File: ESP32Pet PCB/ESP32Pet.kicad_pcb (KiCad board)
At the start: 2 copper layers, 82.3 x 79 mm, 14 parts, among them J2 3.7V LIPO + CHARGING, U1 3.3V LDO, U2 TFT LCD, U5 ESP32-DEVKIT-V1

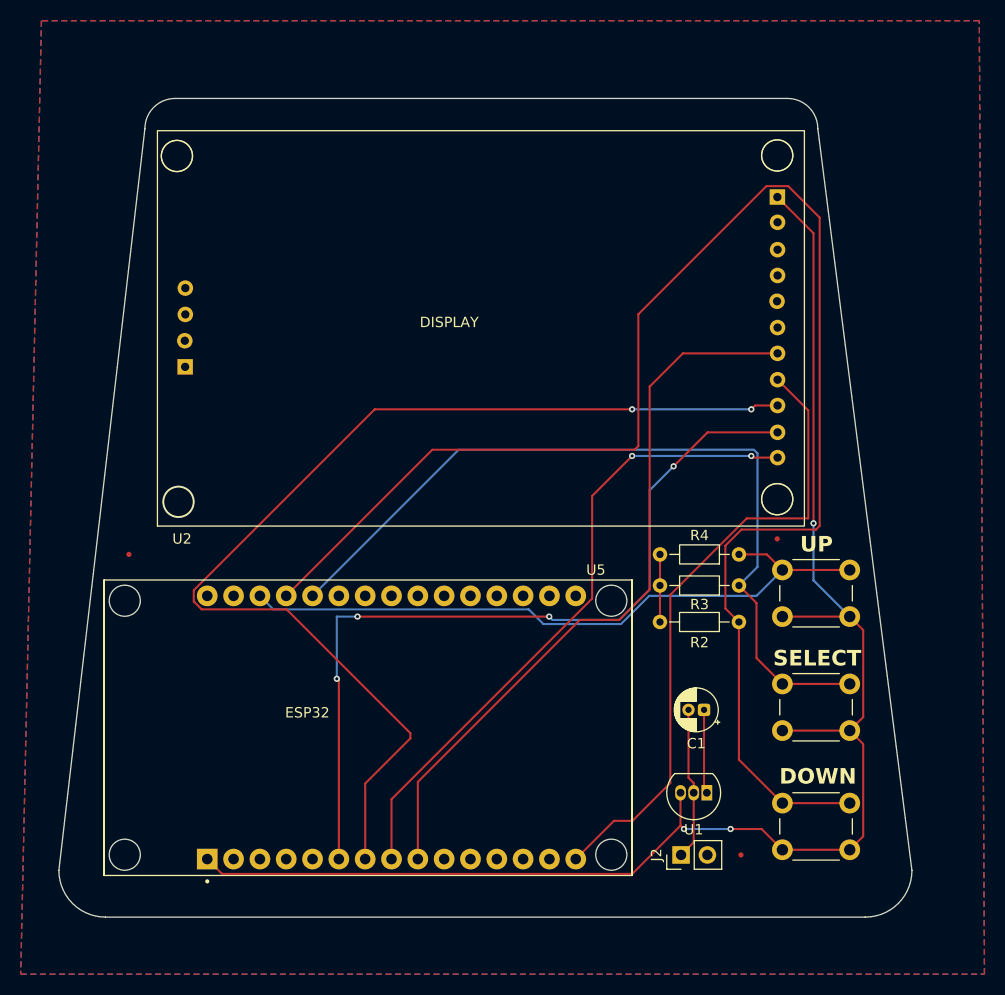
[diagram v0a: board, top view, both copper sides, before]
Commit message: Updated ST7735S Footprint for bigger through holes
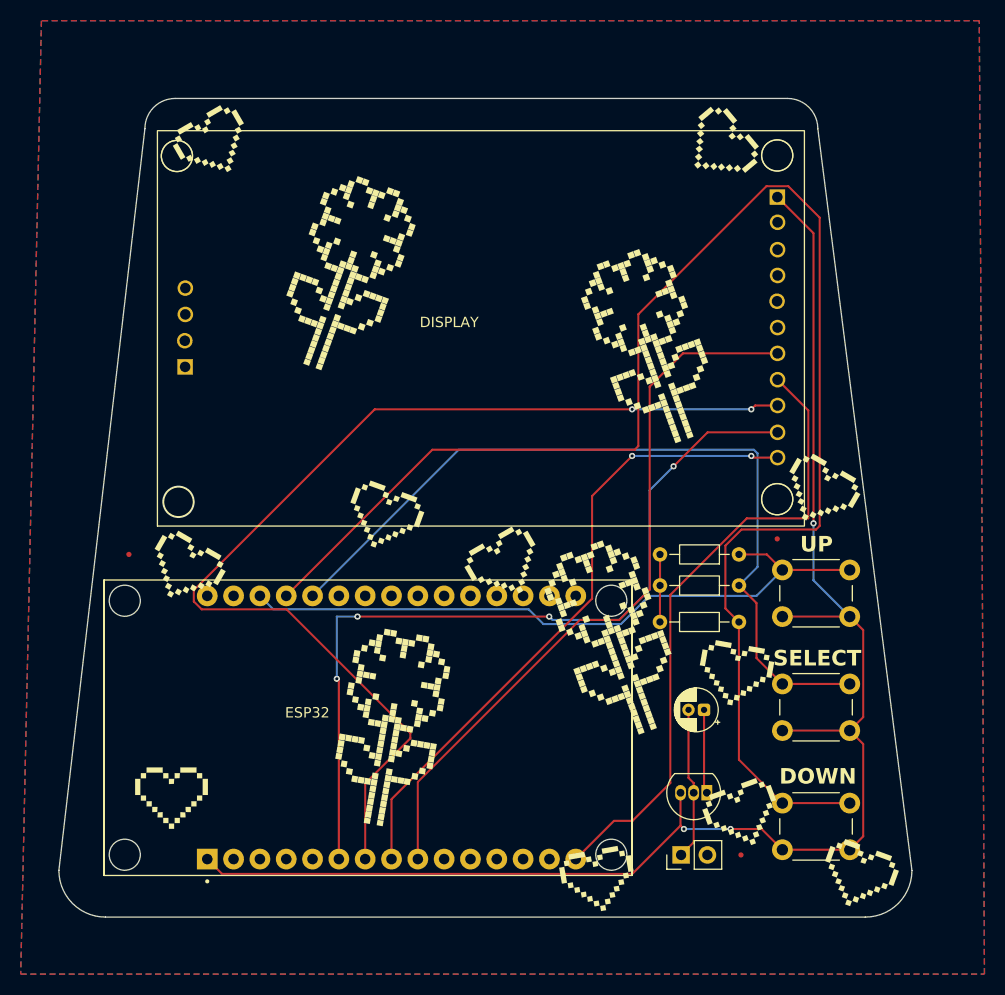
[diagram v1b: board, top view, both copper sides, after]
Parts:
- added REF**: pixel flower, Images:pixel flower, F.Cu at (161.3, 52.1)
- added REF**: pixel heart, Images:pixel heart, F.Cu at (156.7, 104.0)
- added REF**: pixel heart, Images:pixel heart, F.Cu at (178.0, 66.6)
- added REF**: pixel heart, Images:pixel heart, F.Cu at (170.7, 97.7)
- added REF**: pixel heart, Images:pixel heart, F.Cu at (147.8, 73.6)
- added REF**: pixel flower, Images:pixel flower, F.Cu at (157.8, 80.2)
- added REF**: pixel flower, Images:pixel flower, F.Cu at (136.5, 88.6)
- added REF**: pixel heart, Images:pixel heart, B.Cu at (129.4, 34.0)
- added REF**: pixel heart, Images:pixel heart, B.Cu at (121.7, 50.1)
- added REF**: pixel flower, Images:pixel flower, B.Cu at (136.6, 78.6)
- added REF**: pixel flower, Images:pixel flower, B.Cu at (169.1, 42.5)
- added REF**: pixel heart, Images:pixel heart, F.Cu at (181.8, 103.6)
- added REF**: pixel heart, Images:pixel heart, B.Cu at (162.6, 72.6)
- added REF**: pixel heart, Images:pixel heart, B.Cu at (146.8, 84.5)
- added REF**: pixel heart, Images:pixel heart, B.Cu at (155.8, 94.6)
- added REF**: pixel heart, Images:pixel heart, B.Cu at (124.6, 73.4)
- added REF**: pixel heart, Images:pixel heart, B.Cu at (132.9, 49.2)
- added REF**: pixel heart, Images:pixel heart, B.Cu at (125.8, 96.8)
- added REF**: pixel logo, Images:pixel logo, B.Cu at (145.8, 50.2)
- added REF**: pixel heart, Images:pixel heart, B.Cu at (174.2, 77.0)
- added REF**: pixel heart, Images:pixel heart, B.Cu at (156.0, 77.8)
- added REF**: pixel heart, Images:pixel heart, B.Cu at (159.2, 35.4)
- added REF**: pixel flower, Images:pixel flower, F.Cu at (132.3, 44.8)
- added REF**: pixel flower, Images:pixel flower, B.Cu at (172.0, 94.6)
- added REF**: pixel heart, Images:pixel heart, B.Cu at (118.4, 85.6)
- added REF**: pixel heart, Images:pixel heart, F.Cu at (115.6, 96.0)
- added REF**: pixel heart, Images:pixel heart, F.Cu at (169.9, 84.1)
- added REF**: pixel heart, Images:pixel heart, F.Cu at (119.7, 32.9)
- added REF**: pixel heart, Images:pixel heart, F.Cu at (116.8, 74.0)
- added REF**: pixel heart, Images:pixel heart, F.Cu at (168.4, 33.2)
- added REF**: pixel heart, Images:pixel heart, F.Cu at (136.0, 69.0)
